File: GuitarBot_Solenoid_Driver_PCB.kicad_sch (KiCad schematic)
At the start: 46 parts, among them J1 Screw_Terminal_01x02, J2 Screw_Terminal_01x16, J3 Screw_Terminal_01x16, J4 Screw_Terminal_01x04, Q1 NMOS, Q10 NMOS, Q11 NMOS, Q12 NMOS, Q13 NMOS, Q14 NMOS, Q15 NMOS, Q16 NMOS, Q2 NMOS, Q3 NMOS, Q4 NMOS, Q5 NMOS, Q6 NMOS, Q7 NMOS, Q8 NMOS, Q9 NMOS, U1 MCP23017_SP

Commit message: schematic: interrupt and reset pulldown, NMOS gate pulldown, fuses on 12V and 3V3
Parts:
- removed J4: Screw_Terminal_01x04, Connector_PinSocket_2.54mm:PinSocket_1x04_P2.54mm_Vertical, symbol Connector:Screw_Terminal_01x04
- added F1: Polyfuse, symbol Device:Polyfuse
- added F2: Polyfuse_Small, symbol Device:Polyfuse_Small
- added J3V3, JINT1, JMUX: Screw_Terminal_01x02, Connector_Phoenix_MSTB:PhoenixContact_MSTBA_2,5_2-G_1x02_P5.00mm_Horizontal, symbol Connector:Screw_Terminal_01x02
- added R10, R11, R12, R13, R14, R15, R16, R17, R18, R19, R20, R21, R22, R23, R24, R9: 100k, Resistor_THT:R_Axial_DIN0207_L6.3mm_D2.5mm_P7.62mm_Horizontal, symbol Device:R
- added R6, R7, R8: 10k, Resistor_THT:R_Axial_DIN0207_L6.3mm_D2.5mm_P7.62mm_Horizontal, symbol Device:R
- renumbered J1 to J12V, J2 to JSOL1, J3 to JSOL2
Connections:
- net +12V: now also F1.1; no longer C1.1, J12V.1 (Pin_1)
- net +3.3V: now also F2.1, R6.2, R7.1, R8.1; no longer U1.18 (~{RESET}), U1.19 (INTB), U1.20 (INTA)
- net GNDPWR: now also J3V3.2 (Pin_2), R10.1, R11.1, R12.1, R13.1, R14.1, R15.1, R16.1, R17.1, R18.1, R19.1, R20.1, R21.1, R22.1, R23.1, R24.1, R9.1
- net SDA: now also JMUX.1 (Pin_1)
- net SDK: now also JMUX.2 (Pin_2)
- net Sol1: now also R9.2
- net Sol10: now also R18.2
- net Sol11: now also R19.2
- net Sol12: now also R20.2
- net Sol13: now also R21.2
- net Sol14: now also R22.2
- net Sol15: now also R23.2
- net Sol16: now also R24.2
- net Sol2: now also R10.2
- net Sol3: now also R11.2
- net Sol4: now also R12.2
- net Sol5: now also R13.2
- net Sol6: now also R14.2
- net Sol7: now also R15.2
- net Sol8: now also R16.2
- net Sol9: now also R17.2
- new net: JINT1.2 (Pin_2), R8.2, U1.20 (INTA)
- new net: C1.1, F1.2, J12V.1 (Pin_1)
- new net: R6.1, U1.18 (~{RESET})
- new net: F2.2, J3V3.1 (Pin_1)
- new net: JINT1.1 (Pin_1), R7.2, U1.19 (INTB)
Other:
- moved on the sheet: C1, J12V

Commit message: Finished feb15 updates to layout
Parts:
- removed F2: Polyfuse_Small, symbol Device:Polyfuse_Small
- F1: footprint (none) -> Fuse:Fuse_BelFuse_0ZRE0005FF_L8.3mm_W3.8mm
- J3V3, JINT1: footprint Connector_Phoenix_MSTB:PhoenixContact_MSTBA_2,5_2-G_1x02_P5.00mm_Horizontal -> TerminalBlock:TerminalBlock_Xinya_XY308-2.54-2P_1x02_P2.54mm_Horizontal
- JMUX1: renamed from JMUX; footprint Connector_Phoenix_MSTB:PhoenixContact_MSTBA_2,5_2-G_1x02_P5.00mm_Horizontal -> TerminalBlock:TerminalBlock_Xinya_XY308-2.54-2P_1x02_P2.54mm_Horizontal
- JSOL1, JSOL2: footprint Connector_PinSocket_2.54mm:PinSocket_1x16_P2.54mm_Vertical -> TerminalBlock:TerminalBlock_Xinya_XY308-2.54-16P_1x16_P2.54mm_Horizontal
- JSOL_PWR1: renamed from J12V; footprint Connector_Phoenix_MSTB:PhoenixContact_MSTBA_2,5_2-G_1x02_P5.00mm_Horizontal -> TerminalBlock:TerminalBlock_MaiXu_MX126-5.0-02P_1x02_P5.00mm
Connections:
- net +3.3V: now also J3V3.2 (Pin_2)
- net GNDPWR: now also J3V3.1 (Pin_1); no longer J3V3.2 (Pin_2)
- net SDA: now also JMUX1.2 (Pin_2); no longer JMUX1.1 (Pin_1)
- net SDK: now also JMUX1.1 (Pin_1); no longer JMUX1.2 (Pin_2)
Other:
- moved on the sheet: J3V3
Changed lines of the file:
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@@
 	(wire
 		(pts
+			(xy 27.94 40.64) (xy 38.1 40.64)
+		)
+		(stroke
+			(width 0)
+			(type default)
+		)
+	)
+	(wire
+		(pts
 			(xy 224.79 85.09) (xy 246.38 85.09)
 		)
@@
 	(wire
 		(pts
-			(xy 30.48 40.64) (xy 27.94 40.64)
-		)
-		(stroke
-			(width 0)
-			(type default)
-		)
-	)
-	(wire
-		(pts
 			(xy 43.18 130.81) (xy 43.18 128.27)
 		)
@@
 	(wire
 		(pts
-			(xy 35.56 40.64) (xy 38.1 40.64)
-		)
-		(stroke
-			(width 0)
-			(type default)
-		)
-	)
-	(wire
-		(pts
 			(xy 64.77 71.12) (xy 71.12 71.12)
 		)
@@
 		)
 	)
-	(label "SDA"
+	(label "SDK"
 		(at 66.04 40.64 0)
 		(effects
@@
 		)
 	)
-	(label "SDK"
+	(label "SDA"
 		(at 66.04 43.18 0)
 		(effects
@@
 			)
 		)
-		(property "Footprint" ""
+		(property "Footprint" "Fuse:Fuse_BelFuse_0ZRE0005FF_L8.3mm_W3.8mm"
 			(at 31.75 66.04 0)
 			(effects
@@
 		(on_board yes)
 		(dnp no)
-		(property "Reference" "JMUX"
+		(property "Reference" "JMUX1"
 			(at 56.642 38.354 0)
 			(effects
@@
 			)
 		)
-		(property "Footprint" "Connector_Phoenix_MSTB:PhoenixContact_MSTBA_2,5_2-G_1x02_P5.00mm_Horizontal"
+		(property "Footprint" "TerminalBlock:TerminalBlock_Xinya_XY308-2.54-2P_1x02_P2.54mm_Horizontal"
 			(at 57.15 40.64 0)
 			(effects
@@
 			(project "GuitarBot_Solenoid_Driver_PCB"
 				(path "/34c6dfb8-ccfc-4202-9fb2-435617e70f4b"
-					(reference "JMUX")
+					(reference "JMUX1")
 					(unit 1)
 				)
@@
 	)
 	(symbol
-		(lib_id "Device:Polyfuse_Small")
-		(at 33.02 40.64 270)
-		(unit 1)
-		(exclude_from_sim no)
-		(in_bom yes)
-		(on_board yes)
-		(dnp no)
-		(property "Reference" "F2"
-			(at 32.766 38.608 90)
-			(effects
-				(font
-					(size 1.27 1.27)
-				)
-			)
-		)
-		(property "Value" "Polyfuse_Small"
-			(at 33.274 36.83 90)
-			(effects
-				(font
-					(size 1.27 1.27)
-				)
-			)
-		)
-		(property "Footprint" ""
-			(at 27.94 41.91 0)
-			(effects
-				(font
-					(size 1.27 1.27)
-				)
-				(justify left)
-				(hide yes)
-			)
-		)
-		(property "Datasheet" "~"
-			(at 33.02 40.64 0)
-			(effects
-				(font
-					(size 1.27 1.27)
-				)
-				(hide yes)
-			)
-		)
-		(property "Description" "Resettable fuse, polymeric positive temperature coefficient, small symbol"
-			(at 33.02 40.64 0)
-			(effects
-				(font
-					(size 1.27 1.27)
-				)
-				(hide yes)
-			)
-		)
-		(pin "2"
-		)
-		(pin "1"
-		)
-		(instances
-			(project ""
-				(path "/34c6dfb8-ccfc-4202-9fb2-435617e70f4b"
-					(reference "F2")
-					(unit 1)
-				)
-			)
-		)
-	)
-	(symbol
 		(lib_id "Device:R")
 		(at 76.2 139.7 0)
@@
 	(symbol
 		(lib_id "Connector:Screw_Terminal_01x02")
-		(at 22.86 40.64 0)
-		(mirror y)
+		(at 22.86 43.18 180)
 		(unit 1)
 		(exclude_from_sim no)
@@
 		(dnp no)
 		(property "Reference" "J3V3"
-			(at 22.352 38.354 0)
+			(at 22.352 45.466 0)
 			(effects
 				(font
@@
 		)
 		(property "Value" "Screw_Terminal_01x02"
-			(at 22.86 46.736 0)
+			(at 22.86 37.084 0)
 			(effects
 				(font
@@
 			)
 		)
-		(property "Footprint" "Connector_Phoenix_MSTB:PhoenixContact_MSTBA_2,5_2-G_1x02_P5.00mm_Horizontal"
-			(at 22.86 40.64 0)
+		(property "Footprint" "TerminalBlock:TerminalBlock_Xinya_XY308-2.54-2P_1x02_P2.54mm_Horizontal"
+			(at 22.86 43.18 0)
 			(effects
 				(font
@@
 		)
 		(property "Datasheet" "~"
-			(at 22.86 40.64 0)
+			(at 22.86 43.18 0)
 			(effects
 				(font
@@
 		)
 		(property "Description" "Generic screw terminal, single row, 01x02, script generated (kicad-library-utils/schlib/autogen/connector/)"
-			(at 22.86 40.64 0)
+			(at 22.86 43.18 0)
 			(effects
 				(font
@@
 			)
 		)
-		(property "Footprint" "Connector_PinSocket_2.54mm:PinSocket_1x16_P2.54mm_Vertical"
+		(property "Footprint" "TerminalBlock:TerminalBlock_Xinya_XY308-2.54-16P_1x16_P2.54mm_Horizontal"
 			(at 271.78 102.87 0)
 			(effects
@@
 		(dnp no)
 		(fields_autoplaced yes)
-		(property "Reference" "J12V"
+		(property "Reference" "JSOL_PWR1"
 			(at 22.86 64.77 0)
 			(effects
@@
 			)
 		)
-		(property "Footprint" "Connector_Phoenix_MSTB:PhoenixContact_MSTBA_2,5_2-G_1x02_P5.00mm_Horizontal"
+		(property "Footprint" "TerminalBlock:TerminalBlock_MaiXu_MX126-5.0-02P_1x02_P5.00mm"
 			(at 22.86 71.12 0)
 			(effects
@@
 			(project ""
 				(path "/34c6dfb8-ccfc-4202-9fb2-435617e70f4b"
-					(reference "J12V")
+					(reference "JSOL_PWR1")
 					(unit 1)
 				)
@@
 			)
 		)
-		(property "Footprint" "Connector_PinSocket_2.54mm:PinSocket_1x16_P2.54mm_Vertical"
+		(property "Footprint" "TerminalBlock:TerminalBlock_Xinya_XY308-2.54-16P_1x16_P2.54mm_Horizontal"
 			(at 251.46 102.87 0)
 			(effects
@@
 			)
 		)
-		(property "Footprint" "Connector_Phoenix_MSTB:PhoenixContact_MSTBA_2,5_2-G_1x02_P5.00mm_Horizontal"
+		(property "Footprint" "TerminalBlock:TerminalBlock_Xinya_XY308-2.54-2P_1x02_P2.54mm_Horizontal"
 			(at 57.15 107.95 0)
 			(effects

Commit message: initial schematics for ilya rennovations
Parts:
- added C2: 1uF, Capacitor_THT:C_Radial_D10.0mm_H16.0mm_P5.00mm, symbol Device:C
- added H1, H2, H3, H4: MountingHole, MountingHole:MountingHole_3.2mm_M3, symbol Mechanical:MountingHole
- added R25, R26, R27, R28, R29, R30, R31, R32, R33, R34, R35, R36, R37, R38, R39, R40: 100k, Resistor_THT:R_Axial_DIN0207_L6.3mm_D2.5mm_P7.62mm_Horizontal, symbol Device:R
- C1: value 0.1uF -> 1000uF; footprint Capacitor_THT:C_Disc_D5.0mm_W2.5mm_P5.00mm -> Capacitor_THT:CP_Radial_D10.0mm_P5.00mm
- Q1, Q10, Q11, Q12, Q13, Q14, Q15, Q16, Q2, Q3, Q4, Q5, Q6, Q7, Q8, Q9: footprint Package_TO_SOT_THT:TO-220-3_Vertical -> Package_TO_SOT_THT:TO-251-3_Vertical
- R1, R2: value 4k8 -> 4k7
- R10, R11, R12, R13, R14, R15, R16, R17, R18, R19, R20, R21, R22, R23, R24, R9: value 100k -> 100
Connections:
- net +3.3V: now also C2.2
- net GNDPWR: now also C2.1, R25.1, R26.1, R27.1, R28.1, R29.1, R30.1, R31.1, R32.1; no longer R10.1, R11.1, R12.1, R13.1, R14.1, R15.1, R16.1, R17.1, R18.1, R19.1, R20.1, R21.1, R22.1, R23.1, R24.1, R9.1
- net Sol1: no longer names the net of R9.2, U1.21 (GPA0)
- net Sol1: no longer Q1.1 (G)
- net Sol10: no longer names the net of R18.2, U1.2 (GPB1)
- net Sol10: no longer Q10.1 (G)
- net Sol11: no longer names the net of R19.2, U1.3 (GPB2)
- net Sol11: no longer Q11.1 (G)
- net Sol12: no longer names the net of R20.2, U1.4 (GPB3)
- net Sol12: no longer Q12.1 (G)
- net Sol13: no longer names the net of R21.2, U1.5 (GPB4)
- net Sol13: no longer Q13.1 (G)
- net Sol14: no longer names the net of R22.2, U1.6 (GPB5)
- net Sol14: no longer Q14.1 (G)
- net Sol15: no longer names the net of R23.2, U1.7 (GPB6)
- net Sol15: no longer Q15.1 (G)
- net Sol16: no longer names the net of R24.2, U1.8 (GPB7)
- net Sol16: no longer Q16.1 (G)
- net Sol2: no longer names the net of R10.2, U1.22 (GPA1)
- net Sol2: no longer Q2.1 (G)
- net Sol3: no longer names the net of R11.2, U1.23 (GPA2)
- net Sol3: no longer Q3.1 (G)
- net Sol4: no longer names the net of R12.2, U1.24 (GPA3)
- net Sol4: no longer Q4.1 (G)
- net Sol5: no longer names the net of R13.2, U1.25 (GPA4)
- net Sol5: no longer Q5.1 (G)
- net Sol6: no longer names the net of R14.2, U1.26 (GPA5)
- net Sol6: no longer Q6.1 (G)
- net Sol7: no longer names the net of R15.2, U1.27 (GPA6)
- net Sol7: no longer Q7.1 (G)
- net Sol8: no longer names the net of R16.2, U1.28 (GPA7)
- net Sol8: no longer Q8.1 (G)
- net Sol9: no longer names the net of R17.2, U1.1 (GPB0)
- net Sol9: no longer Q9.1 (G)
- new net SOL_GATE1: Q1.1 (G), R25.2, R9.1
- new net SOL_GATE10: Q10.1 (G), R18.1, R34.2
- new net SOL_GATE11: Q11.1 (G), R19.1, R35.2
- new net SOL_GATE12: Q12.1 (G), R20.1, R36.2
- new net SOL_GATE13: Q13.1 (G), R21.1, R37.2
- new net SOL_GATE14: Q14.1 (G), R22.1, R38.2
- new net SOL_GATE15: Q15.1 (G), R23.1, R39.2
- new net SOL_GATE16: Q16.1 (G), R24.1, R40.2
- new net SOL_GATE2: Q2.1 (G), R10.1, R26.2
- new net SOL_GATE3: Q3.1 (G), R11.1, R27.2
- new net SOL_GATE4: Q4.1 (G), R12.1, R28.2
- new net SOL_GATE5: Q5.1 (G), R13.1, R29.2
- new net SOL_GATE6: Q6.1 (G), R14.1, R30.2
- new net SOL_GATE7: Q7.1 (G), R15.1, R31.2
- new net SOL_GATE8: Q8.1 (G), R16.1, R32.2
- new net SOL_GATE9: Q9.1 (G), R17.1, R33.2
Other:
- moved on the sheet: D1, D10, D11, D12, D13, D14, D15, D16, D2, D3, D4, D5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

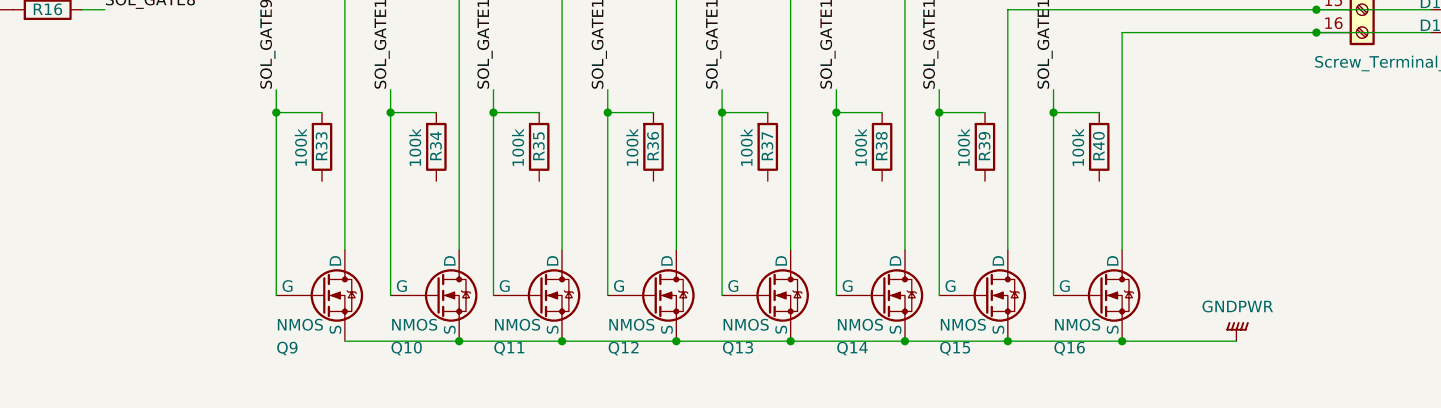
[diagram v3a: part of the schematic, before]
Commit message: Fixed connectection issue with resistors
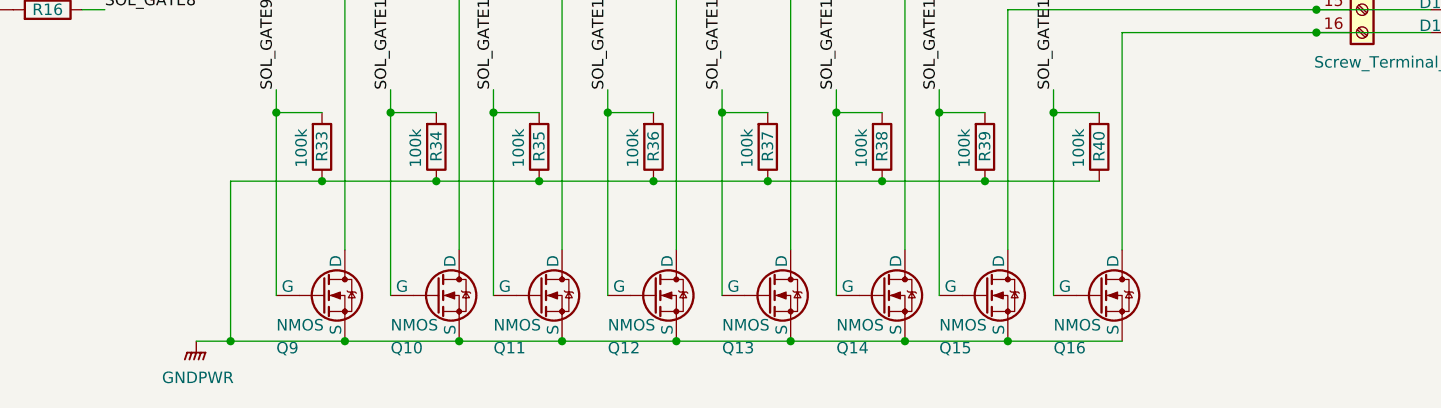
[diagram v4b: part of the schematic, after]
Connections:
- net GNDPWR: now also R33.1, R34.1, R35.1, R36.1, R37.1, R38.1, R39.1, R40.1
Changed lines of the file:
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@@
 	)
 	(junction
+		(at 142.24 139.7)
+		(diameter 0)
+		(color 0 0 0 0)
+	)
+	(junction
 		(at 283.21 95.25)
 		(diameter 0)
@@
 	)
 	(junction
+		(at 179.07 139.7)
+		(diameter 0)
+		(color 0 0 0 0)
+	)
+	(junction
 		(at 252.73 115.57)
 		(diameter 0)
@@
 	)
 	(junction
+		(at 215.9 139.7)
+		(diameter 0)
+		(color 0 0 0 0)
+	)
+	(junction
 		(at 252.73 85.09)
 		(diameter 0)
@@
 	)
 	(junction
+		(at 191.77 139.7)
+		(diameter 0)
+		(color 0 0 0 0)
+	)
+	(junction
 		(at 207.01 157.48)
 		(diameter 0)
@@
 	)
 	(junction
+		(at 166.37 139.7)
+		(diameter 0)
+		(color 0 0 0 0)
+	)
+	(junction
 		(at 189.23 72.39)
 		(diameter 0)
@@
 	)
 	(junction
+		(at 204.47 139.7)
+		(diameter 0)
+		(color 0 0 0 0)
+	)
+	(junction
 		(at 173.99 132.08)
 		(diameter 0)
@@
 	)
 	(junction
-		(at 231.14 157.48)
+		(at 147.32 64.77)
 		(diameter 0)
 		(color 0 0 0 0)
 	)
 	(junction
-		(at 147.32 64.77)
+		(at 144.78 50.8)
 		(diameter 0)
 		(color 0 0 0 0)
 	)
 	(junction
-		(at 144.78 50.8)
+		(at 186.69 132.08)
 		(diameter 0)
 		(color 0 0 0 0)
 	)
 	(junction
-		(at 186.69 132.08)
+		(at 154.94 139.7)
 		(diameter 0)
 		(color 0 0 0 0)
@@
 	)
 	(junction
+		(at 132.08 157.48)
+		(diameter 0)
+		(color 0 0 0 0)
+	)
+	(junction
 		(at 283.21 105.41)
 		(diameter 0)
@@
 	)
 	(junction
+		(at 144.78 157.48)
+		(diameter 0)
+		(color 0 0 0 0)
+	)
+	(junction
 		(at 137.16 50.8)
 		(diameter 0)
@@
 	(wire
 		(pts
+			(xy 215.9 139.7) (xy 228.6 139.7)
+		)
+		(stroke
+			(width 0)
+			(type default)
+		)
+	)
+	(wire
+		(pts
 			(xy 207.01 60.96) (xy 207.01 90.17)
 		)
@@
 	(wire
 		(pts
+			(xy 191.77 139.7) (xy 204.47 139.7)
+		)
+		(stroke
+			(width 0)
+			(type default)
+		)
+	)
+	(wire
+		(pts
 			(xy 189.23 55.88) (xy 189.23 72.39)
 		)
@@
 	(wire
 		(pts
+			(xy 142.24 139.7) (xy 154.94 139.7)
+		)
+		(stroke
+			(width 0)
+			(type default)
+		)
+	)
+	(wire
+		(pts
 			(xy 181.61 157.48) (xy 194.31 157.48)
 		)
@@
 	(wire
 		(pts
+			(xy 204.47 139.7) (xy 215.9 139.7)
+		)
+		(stroke
+			(width 0)
+			(type default)
+		)
+	)
+	(wire
+		(pts
 			(xy 252.73 118.11) (xy 265.43 118.11)
 		)
@@
 	(wire
 		(pts
+			(xy 128.27 157.48) (xy 132.08 157.48)
+		)
+		(stroke
+			(width 0)
+			(type default)
+		)
+	)
+	(wire
+		(pts
 			(xy 165.1 55.88) (xy 165.1 72.39)
 		)
@@
 	(wire
 		(pts
+			(xy 154.94 139.7) (xy 166.37 139.7)
+		)
+		(stroke
+			(width 0)
+			(type default)
+		)
+	)
+	(wire
+		(pts
 			(xy 27.94 40.64) (xy 38.1 40.64)
 		)
@@
 	(wire
 		(pts
+			(xy 166.37 139.7) (xy 179.07 139.7)
+		)
+		(stroke
+			(width 0)
+			(type default)
+		)
+	)
+	(wire
+		(pts
 			(xy 168.91 147.32) (xy 168.91 110.49)
 		)
@@
 	(wire
 		(pts
+			(xy 142.24 139.7) (xy 132.08 139.7)
+		)
+		(stroke
+			(width 0)
+			(type default)
+		)
+	)
+	(wire
+		(pts
 			(xy 137.16 50.8) (xy 132.08 50.8)
 		)
@@
 	(wire
 		(pts
+			(xy 132.08 139.7) (xy 132.08 157.48)
+		)
+		(stroke
+			(width 0)
+			(type default)
+		)
+	)
+	(wire
+		(pts
 			(xy 67.31 82.55) (xy 72.39 82.55)
 		)
@@
 	(wire
 		(pts
-			(xy 231.14 157.48) (xy 243.84 157.48)
-		)
-		(stroke
-			(width 0)
-			(type default)
-		)
-	)
-	(wire
-		(pts
 			(xy 273.05 90.17) (xy 273.05 92.71)
 		)
@@
 	(wire
 		(pts
+			(xy 179.07 139.7) (xy 191.77 139.7)
+		)
+		(stroke
+			(width 0)
+			(type default)
+		)
+	)
+	(wire
+		(pts
 			(xy 168.91 50.8) (xy 181.61 50.8)
 		)
@@
 	(wire
 		(pts
+			(xy 132.08 157.48) (xy 144.78 157.48)
+		)
+		(stroke
+			(width 0)
+			(type default)
+		)
+	)
+	(wire
+		(pts
 			(xy 62.23 130.81) (xy 62.23 132.08)
 		)
@@
 	(symbol
 		(lib_id "power:GNDPWR")
-		(at 243.84 157.48 180)
+		(at 128.27 157.48 0)
 		(unit 1)
 		(exclude_from_sim no)
@@
 		(on_board yes)
 		(dnp no)
-		(fields_autoplaced yes)
 		(property "Reference" "#PWR04"
-			(at 243.84 152.4 0)
+			(at 128.27 162.56 0)
 			(effects
 				(font
@@
 		)
 		(property "Value" "GNDPWR"
-			(at 243.967 153.67 0)
+			(at 124.46 161.544 0)
 			(effects
 				(font
 					(size 1.27 1.27)
 				)
+				(justify left)
 			)
 		)
 		(property "Footprint" ""
-			(at 243.84 156.21 0)
+			(at 128.27 158.75 0)
 			(effects
 				(font
@@
 		)
 		(property "Datasheet" ""
-			(at 243.84 156.21 0)
+			(at 128.27 158.75 0)
 			(effects
 				(font
@@
 		)
 		(property "Description" "Power symbol creates a global label with name \"GNDPWR\" , global ground"
-			(at 243.84 157.48 0)
+			(at 128.27 157.48 0)
 			(effects
 				(font

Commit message: changed 01x16 terminal blocks from 2.54mm to 5.08mm
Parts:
- JSOL1, JSOL2: footprint TerminalBlock:TerminalBlock_Xinya_XY308-2.54-16P_1x16_P2.54mm_Horizontal -> TerminalBlock_CUI:TerminalBlock_CUI_TB007-508-16_1x16_P5.08mm_Horizontal
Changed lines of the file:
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@@
 			)
 		)
-		(property "Footprint" "TerminalBlock:TerminalBlock_Xinya_XY308-2.54-16P_1x16_P2.54mm_Horizontal"
+		(property "Footprint" "TerminalBlock_CUI:TerminalBlock_CUI_TB007-508-16_1x16_P5.08mm_Horizontal"
 			(at 278.13 102.87 0)
 			(effects
@@
 			)
 		)
-		(property "Footprint" "TerminalBlock:TerminalBlock_Xinya_XY308-2.54-16P_1x16_P2.54mm_Horizontal"
+		(property "Footprint" "TerminalBlock_CUI:TerminalBlock_CUI_TB007-508-16_1x16_P5.08mm_Horizontal"
 			(at 257.81 102.87 0)
 			(effects

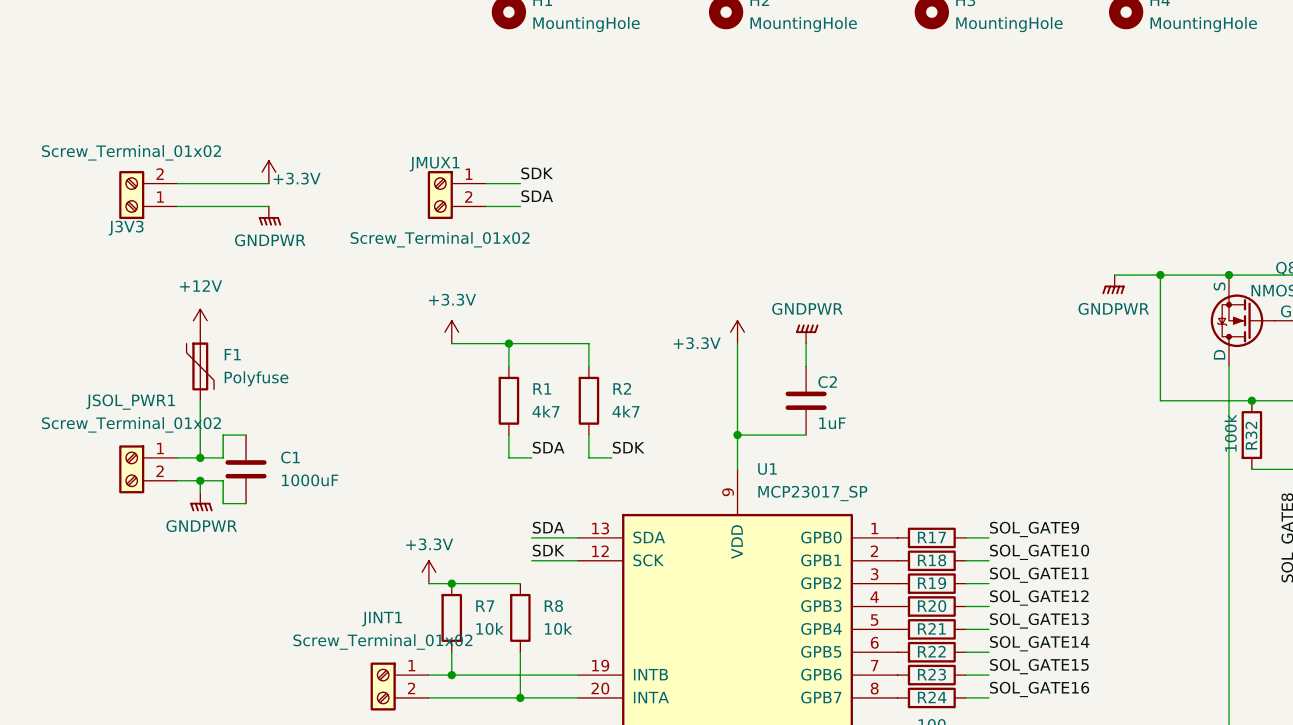
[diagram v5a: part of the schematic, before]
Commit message: Minimal changes to naming
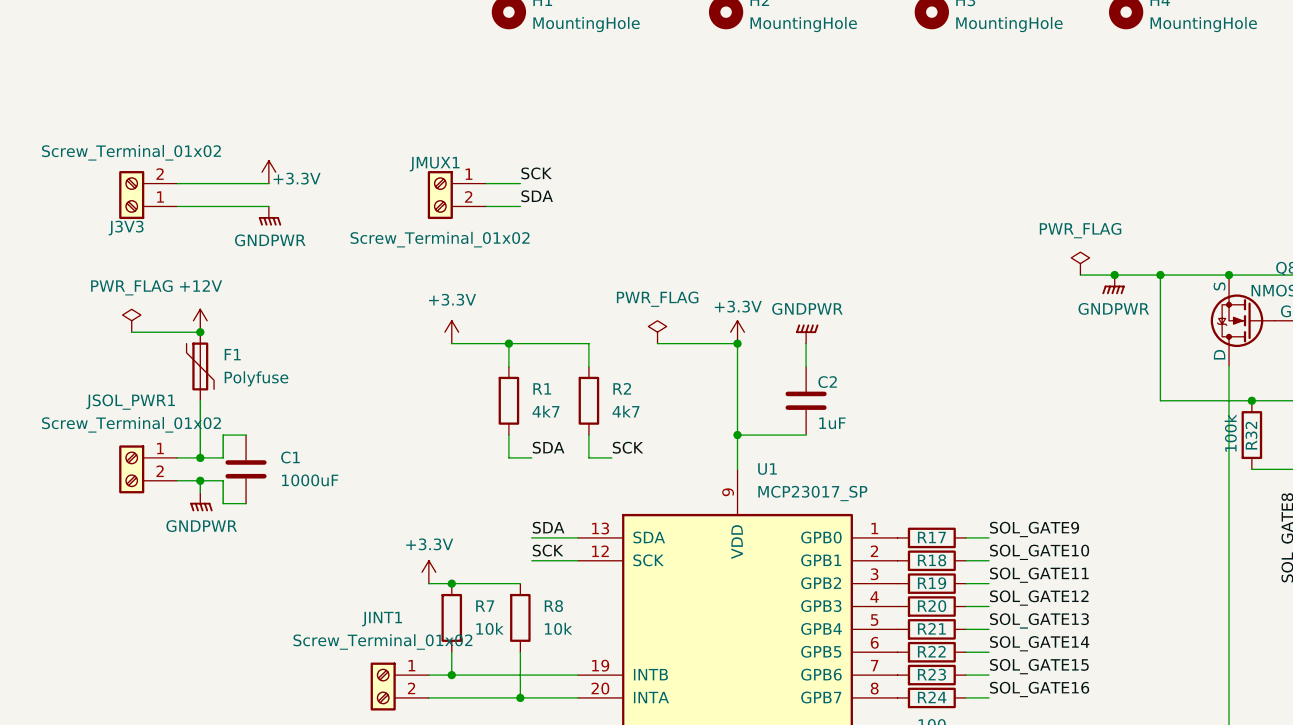
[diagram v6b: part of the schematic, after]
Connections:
- net SDK renamed SCK
